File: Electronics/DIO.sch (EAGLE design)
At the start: 6 parts

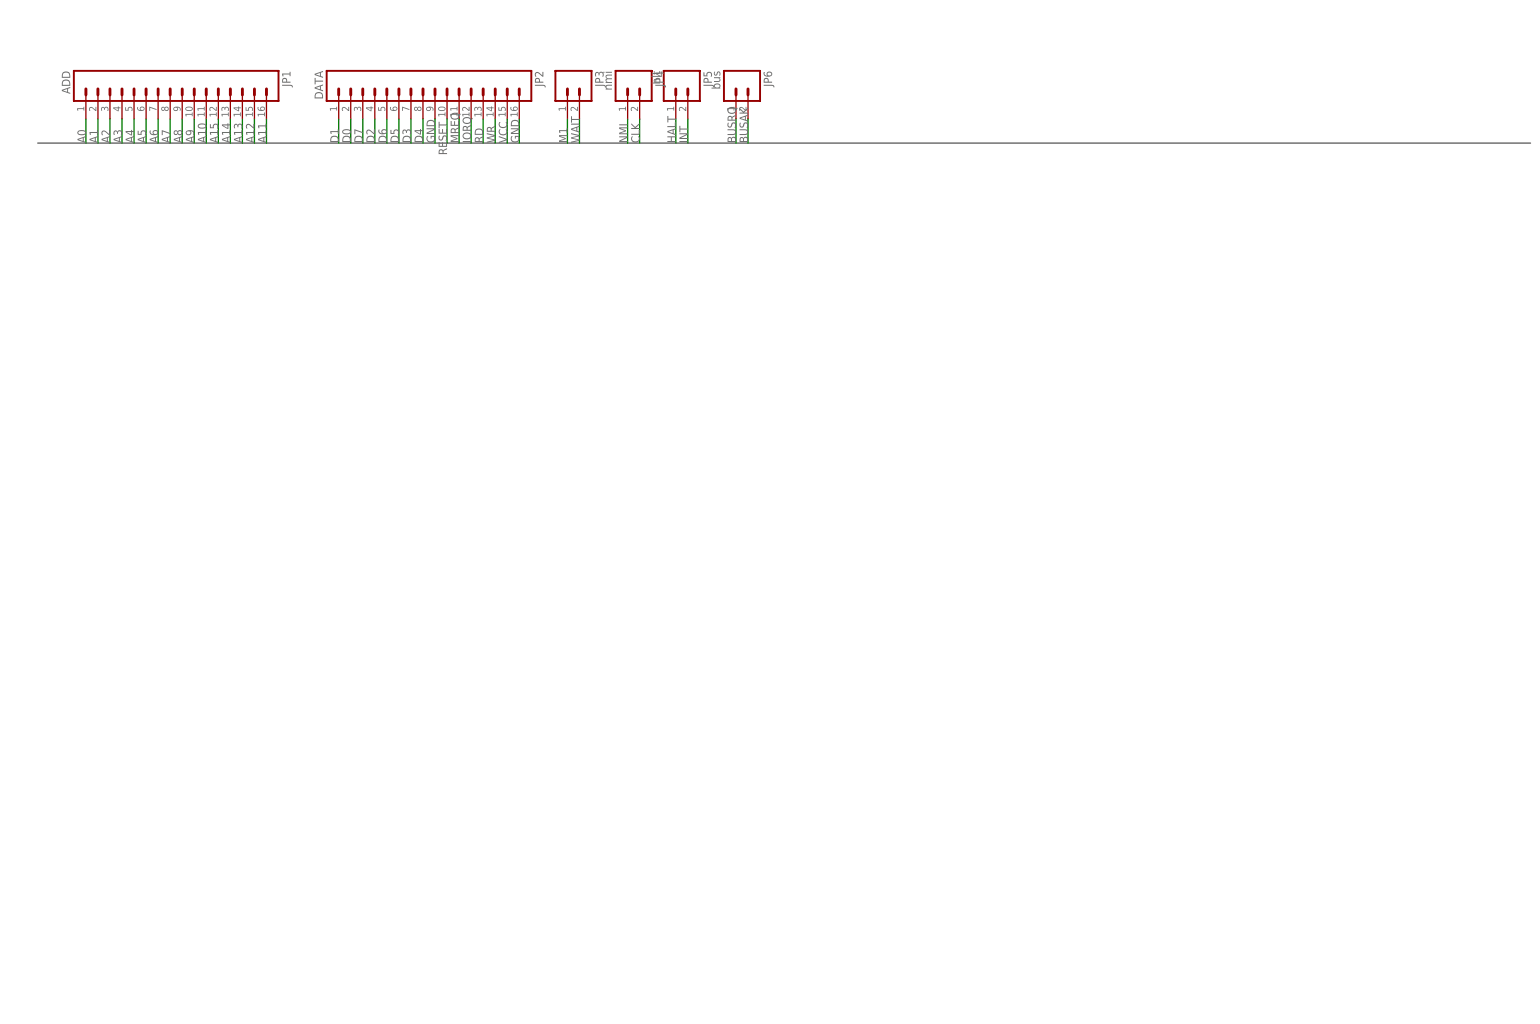
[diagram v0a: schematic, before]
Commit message: Route DIO Breakout + update Text
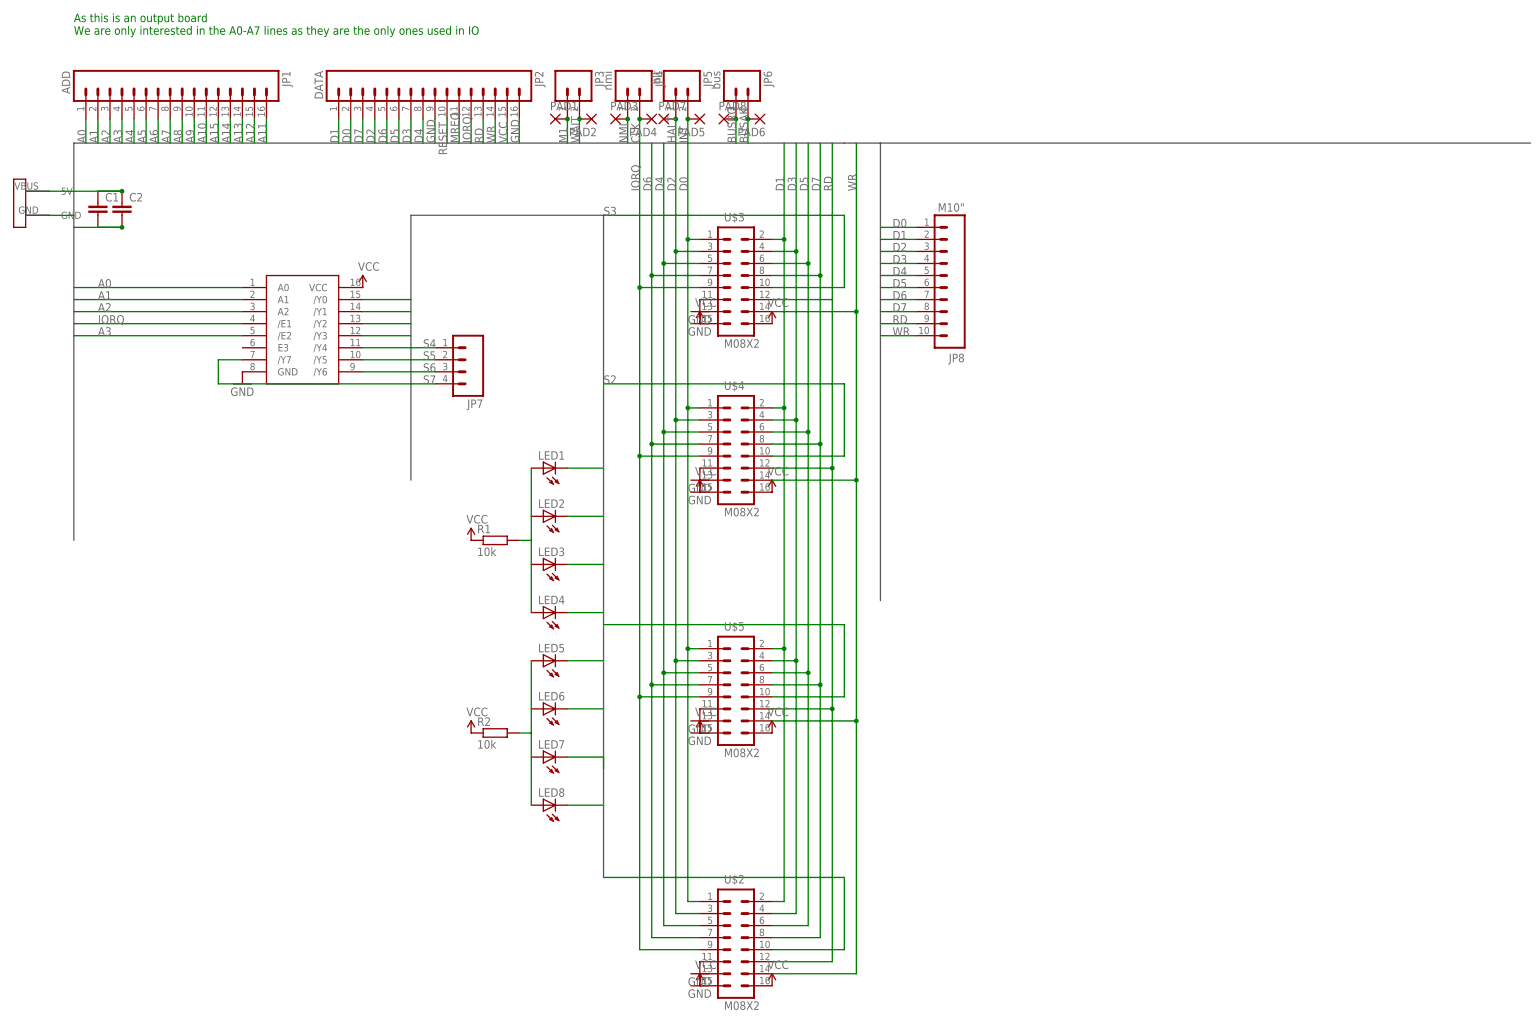
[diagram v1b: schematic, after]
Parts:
- added C1, C2: (no value), rcl:C-EUC0805
- added JP7: (no value), SparkFun-Connectors:M04PTH
- added JP8: M10", SparkFun:M10"
- added LED1, LED2, LED3, LED4, LED5, LED6, LED7, LED8: (no value), adafruit:LEDCHIP-LED0805
- added PAD1, PAD2, PAD3, PAD4, PAD5, PAD6, PAD7, PAD8: (no value), wirepad:SMD2
- added R1, R2: 10k, rcl:R-EU_M0805
- added U$1: 74LVC138AD, SparkFun-DigitalIC:74LVC138AD
- added U$2, U$3, U$4, U$5: M08X2, SparkFun-Connectors:M08X2
- added U$6: USB-MICRO-PWR, RalimTek:USB-MICRO-PWR
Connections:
- new net N$1: LED1.A, LED2.A, LED3.A, LED4.A, R1.2
- new net N$2: LED5.A, LED6.A, LED7.A, LED8.A, R2.2
- new net S0: LED1.C, U$1./Y0, U$2.10
- new net S1: LED2.C, U$1./Y1, U$5.10
- new net S2: LED3.C, U$1./Y2, U$4.10
- new net S3: LED4.C, U$1./Y3, U$3.10
- new net S4: JP7.1, LED5.C, U$1./Y4
- new net S5: JP7.2, LED6.C, U$1./Y5
- new net S6: JP7.3, LED7.C, U$1./Y6
- new net S7: JP7.4, LED8.C, U$1./Y7
- net A0: now also U$1.A0
- net A1: now also U$1.A1
- net A2: now also U$1.A2
- net A3: now also U$1./E2
- net BUSAK: now also PAD6.P
- net BUSRQ: now also PAD8.P
- net CLK: now also PAD4.P
- net D0: now also JP8.1, U$2.1, U$3.1, U$4.1, U$5.1
- net D1: now also JP8.2, U$2.2, U$3.2, U$4.2, U$5.2
- net D2: now also JP8.3, U$2.3, U$3.3, U$4.3, U$5.3
- net D3: now also JP8.4, U$2.4, U$3.4, U$4.4, U$5.4
- net D4: now also JP8.5, U$2.5, U$3.5, U$4.5, U$5.5
- net D5: now also JP8.6, U$2.6, U$3.6, U$4.6, U$5.6
- net D6: now also JP8.7, U$2.7, U$3.7, U$4.7, U$5.7
- net D7: now also JP8.8, U$2.8, U$3.8, U$4.8, U$5.8
- net GND: now also C1.2, C2.2, U$1.GND, U$2.11, U$2.13, U$3.11, U$3.13, U$4.11, U$4.13, U$5.11, U$5.13, U$6.GND
- net HALT: now also PAD7.P
- net INT: now also PAD5.P
- net IORQ: now also U$1./E1, U$2.9, U$3.9, U$4.9, U$5.9
- net M1: now also PAD1.P
- net NMI: now also PAD3.P
- net RD: now also JP8.9, U$2.12, U$3.12, U$4.12, U$5.12
- net VCC: now also C1.1, C2.1, R1.1, R2.1, U$1.VCC, U$2.15, U$2.16, U$3.15, U$3.16, U$4.15, U$4.16, U$5.15, U$5.16, U$6.5V
- net WAIT: now also PAD2.P
- net WR: now also JP8.10, U$2.14, U$3.14, U$4.14, U$5.14
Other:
- note added: "As this is an output board We are only interested in the A0-A7 lines as they are the only ones used in IO"
